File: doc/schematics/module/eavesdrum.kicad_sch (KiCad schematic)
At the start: 96 parts, among them J1 DC37_Pins_MountingHoles, J2 Conn_02x25_Odd_Even, J3 Conn_01x03, SW1 SW_Push, SW2 SW_Push, SW3 SW_Push, U1 CD74HC4067M, U2 CD74HC4067M

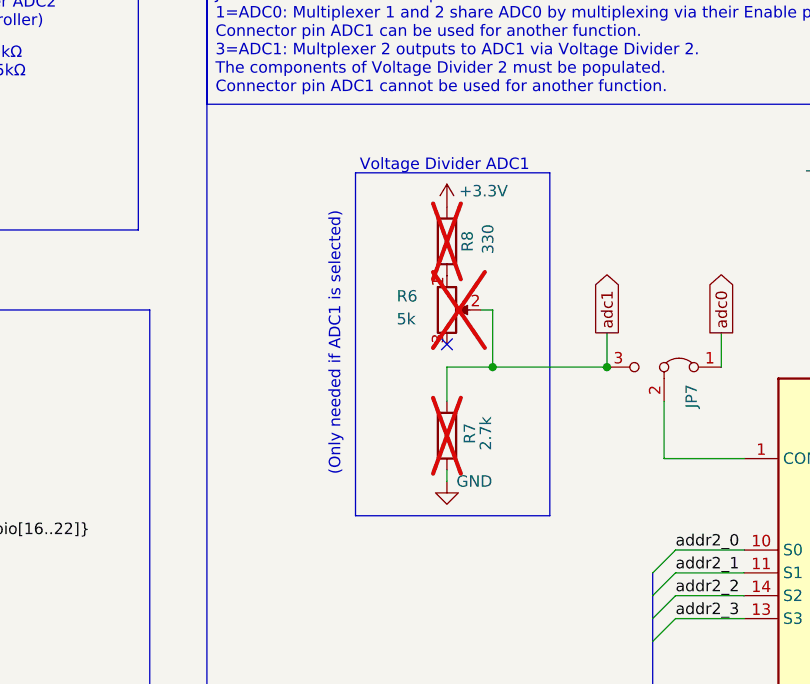
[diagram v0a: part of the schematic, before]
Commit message: adjust module schematics
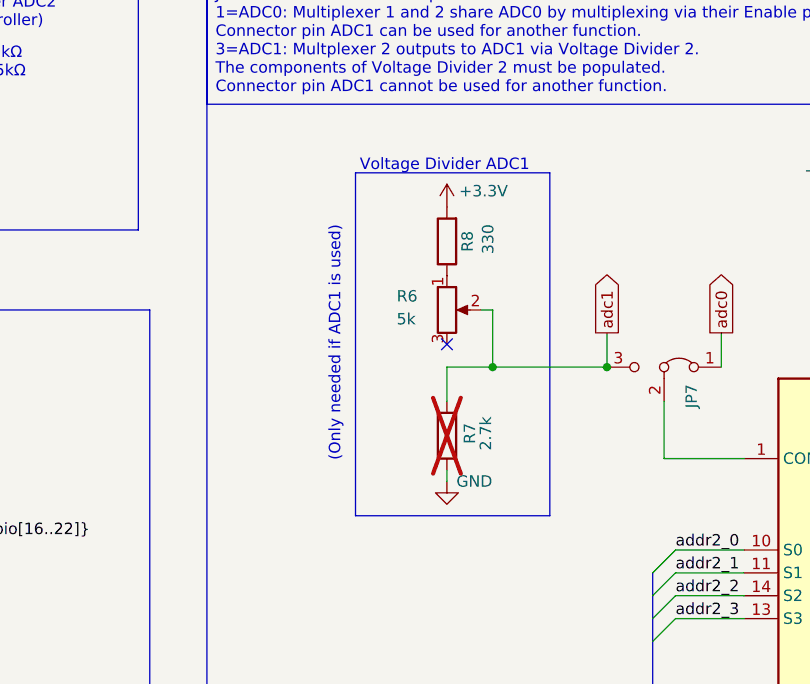
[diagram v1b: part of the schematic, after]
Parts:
- R6, R8: now fitted; now in the parts list
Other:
- note added: "(Only needed if ADC1 is used)"
- note removed: "(Only needed if ADC1 is selected)"
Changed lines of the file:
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@@
 		)
 	)
-	(text "(Only needed if ADC1 is selected)"
+	(text "(Only needed if ADC1 is used)"
 		(exclude_from_sim no)
 		(at 195.834 157.48 90)
@@
 		(unit 1)
 		(exclude_from_sim no)
-		(in_bom no)
+		(in_bom yes)
 		(on_board yes)
-		(dnp yes)
+		(dnp no)
 		(property "Reference" "R6"
 			(at 202.692 152.146 0)
@@
 		(unit 1)
 		(exclude_from_sim no)
-		(in_bom no)
+		(in_bom yes)
 		(on_board yes)
-		(dnp yes)
+		(dnp no)
 		(property "Reference" "R8"
 			(at 210.566 146.05 90)
